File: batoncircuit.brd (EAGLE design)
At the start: 105.1 x 31.7 mm, 19 parts, among them IC1 74LS595D, IC2 4543D, IC3 4543D, IC5 RFD22301, IC6 TLC555CD, IC8-LP3872 786TV, U8 V321-3DIGIT-LCD

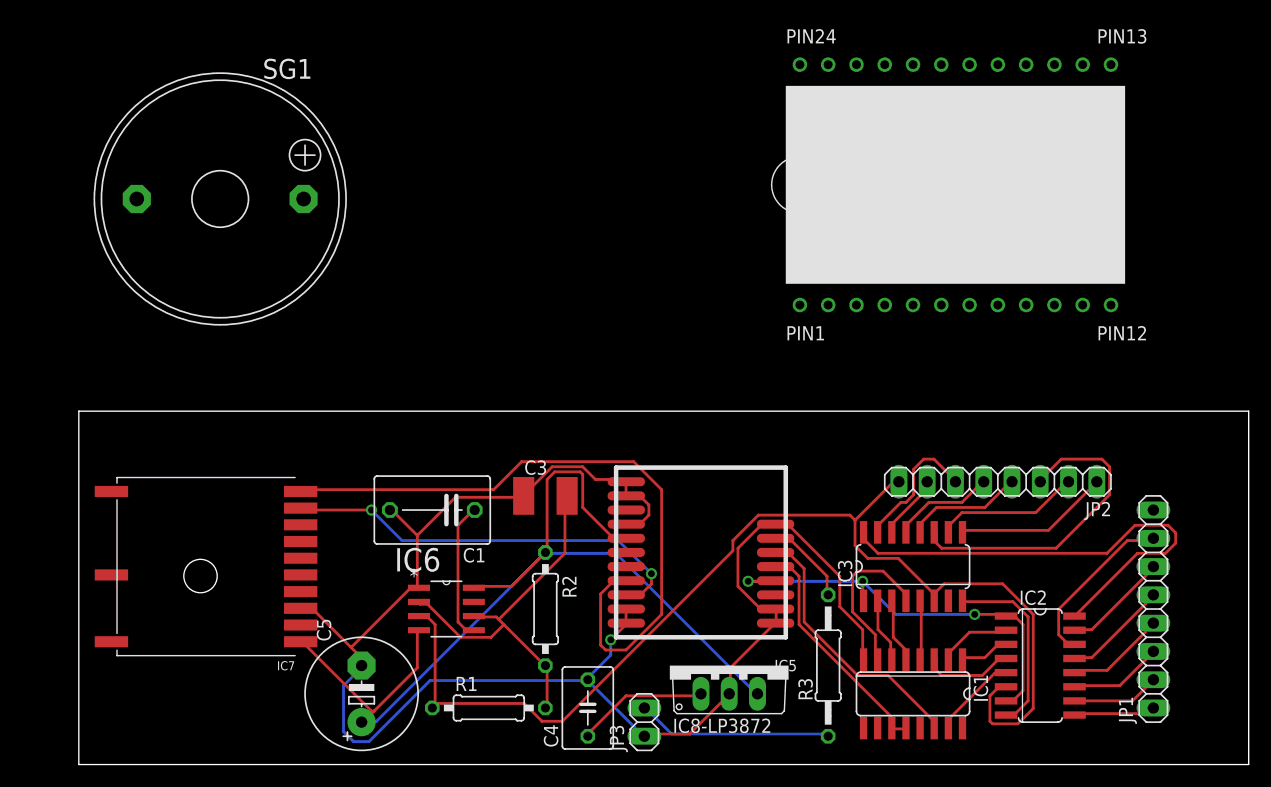
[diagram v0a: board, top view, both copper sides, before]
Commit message: Switches and jack addition
Added power jack, marker switch and power switch along with connecting
pins on board.
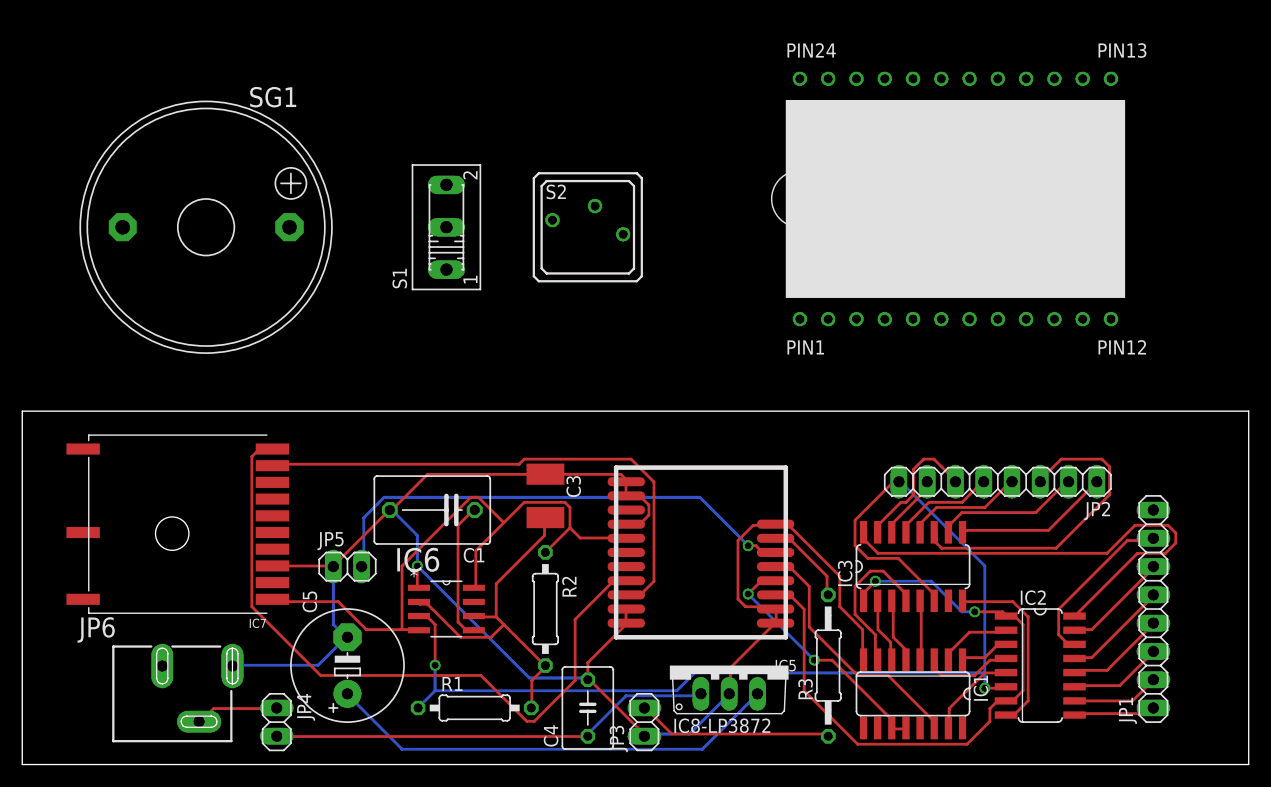
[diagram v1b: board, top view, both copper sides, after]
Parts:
- added JP4, JP5: (no value), pinhead:1X02
- added JP6: POWER_JACKSLT, SparkFun-Connectors:POWER_JACK_SLOT
- added S1: (no value), switch:255SB
- added S2: RDT1034, switch:RDT1034
- moved IC7 4.58 mm to (8.89, 21.6)
- moved C5 2.84 mm to (24.1, 8.89)
- moved SG1 2.84 mm to (11.4, 48.3)
- moved U8 1.27 mm to (78.7, 50.8)
- moved R1 1.27 mm to (35.6, 5.08)
- turned C3 to 270 degrees
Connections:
- new net N$51: C5.+, IC8-LP3872.3
- new net N$52: JP4.1, JP6.GND@2
- new net N$53: S1.3
- new net N$54: S1.2
- new net N$55: IC5.6, JP5.2
- new net N$56: S2.B
- new net N$57: S2.A
- net +3V3: no longer C5.+, IC8-LP3872.3
- net GND: now also JP5.1, JP6.PWR
- net N$24: now also IC5.5; no longer IC5.6
- net N$29: now also IC5.3; no longer IC5.4
- net N$31: now also JP4.2
- net N$34: now also IC5.4; no longer IC5.5
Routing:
- net N$55: track 0.00 -> 44.3 mm, vias 0 -> 1
- net N$51: track 0.00 -> 41.0 mm
- net +3V3: track 92.6 -> 56.9 mm
- net N$31: track 11.9 -> 39.9 mm
- net N$29: track 38.4 -> 57.8 mm, vias 3 -> 2
- net N$28: track 37.5 -> 47.2 mm, vias 2 -> 0
- net N$52: track 0.00 -> 7.46 mm
- net GND: track 146.2 -> 151.4 mm
- net N$27: track 35.3 -> 32.8 mm
- net N$26: track 60.2 -> 62.1 mm
- net N$34: track 21.0 -> 22.6 mm, vias 0 -> 2
- net N$24: track 23.9 -> 22.8 mm
- net N$23: track 101.9 -> 100.9 mm, vias 0 -> 2
- net N$19: track 14.9 -> 14.0 mm
- net N$15: track 7.67 -> 8.21 mm
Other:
- board size 105.1 x 31.7 mm -> 110.2 x 31.7 mm
